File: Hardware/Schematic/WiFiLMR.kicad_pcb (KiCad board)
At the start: 2 copper layers, 26 parts, among them J1 Conn_01x12, J2 Conn_01x12, J3 JTAG, J4 Conn_02x04_Odd_Even, J5 Conn_02x02_Odd_Even, J6 Conn_01x12, J7 Conn_01x12, U1 TCA8418RTWR

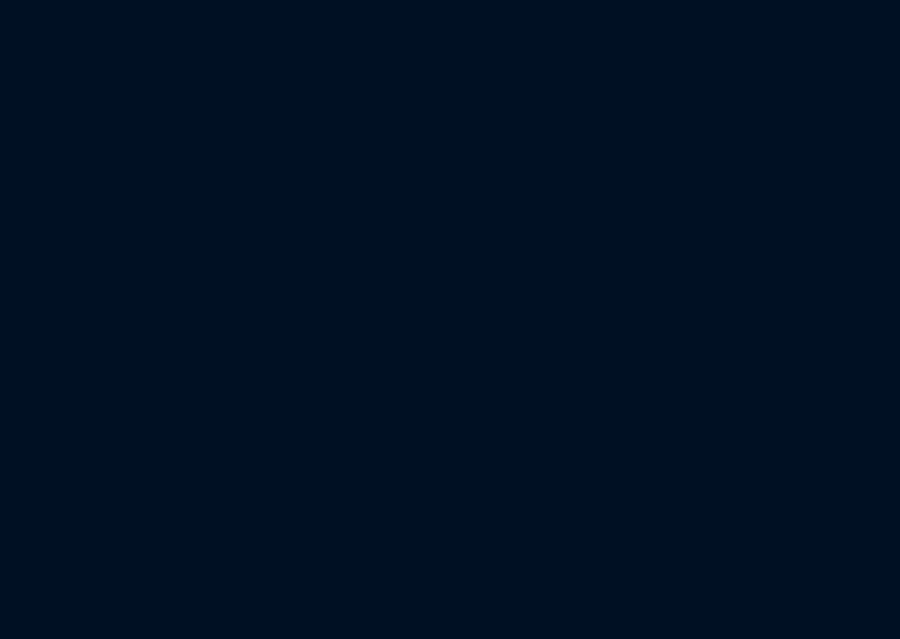
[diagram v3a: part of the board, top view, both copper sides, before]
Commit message: Added E-INK display connector and datasheet
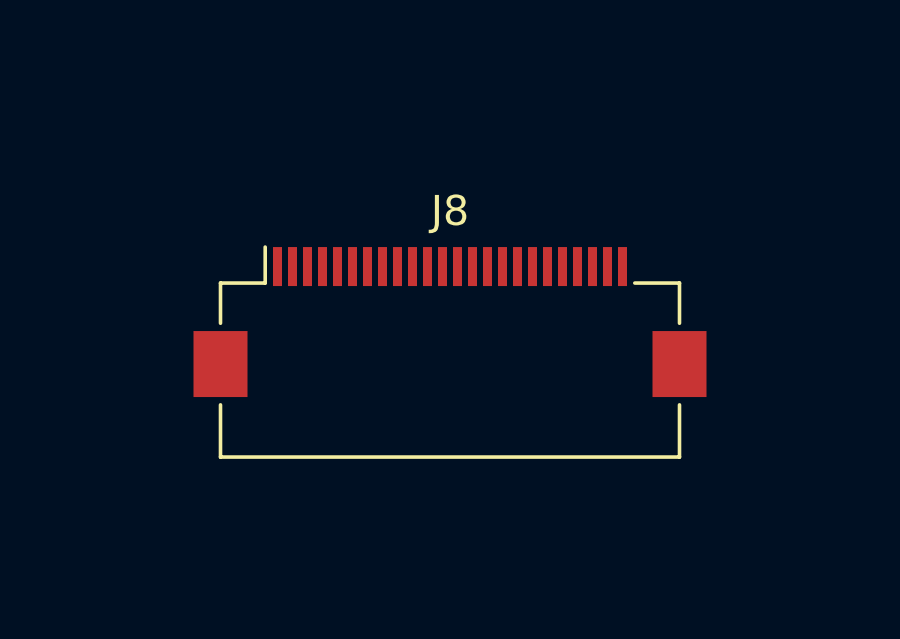
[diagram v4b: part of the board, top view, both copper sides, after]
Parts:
- added J8: Conn_01x24, Connector_FFC-FPC:Hirose_FH12-24S-0.5SH_1x24-1MP_P0.50mm_Horizontal, F.Cu at (74.9, 137.2)
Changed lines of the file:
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@@
     (tracks 0)
     (zones 0)
-    (modules 26)
-    (nets 103)
+    (modules 27)
+    (nets 127)
   )
   (page A4)
@@
   (net 101 /Keypad/COL9)
   (net 102 /Keypad/ROW7)
+  (net 103 "Net-(J8-Pad24)")
+  (net 104 "Net-(J8-Pad23)")
+  (net 105 "Net-(J8-Pad22)")
+  (net 106 "Net-(J8-Pad21)")
+  (net 107 "Net-(J8-Pad20)")
+  (net 108 "Net-(J8-Pad19)")
+  (net 109 "Net-(J8-Pad18)")
+  (net 110 "Net-(J8-Pad17)")
+  (net 111 "Net-(J8-Pad16)")
+  (net 112 "Net-(J8-Pad15)")
+  (net 113 "Net-(J8-Pad14)")
+  (net 114 "Net-(J8-Pad13)")
+  (net 115 "Net-(J8-Pad12)")
+  (net 116 "Net-(J8-Pad11)")
+  (net 117 "Net-(J8-Pad10)")
+  (net 118 "Net-(J8-Pad9)")
+  (net 119 "Net-(J8-Pad8)")
+  (net 120 "Net-(J8-Pad7)")
+  (net 121 "Net-(J8-Pad6)")
+  (net 122 "Net-(J8-Pad5)")
+  (net 123 "Net-(J8-Pad4)")
+  (net 124 "Net-(J8-Pad3)")
+  (net 125 "Net-(J8-Pad2)")
+  (net 126 "Net-(J8-Pad1)")
   (net_class Default "This is the default net class."
     (clearance 0.2)
@@
     (add_net "Net-(J7-Pad12)")
     (add_net "Net-(J7-Pad9)")
+    (add_net "Net-(J8-Pad1)")
+    (add_net "Net-(J8-Pad10)")
+    (add_net "Net-(J8-Pad11)")
+    (add_net "Net-(J8-Pad12)")
+    (add_net "Net-(J8-Pad13)")
+    (add_net "Net-(J8-Pad14)")
+    (add_net "Net-(J8-Pad15)")
+    (add_net "Net-(J8-Pad16)")
+    (add_net "Net-(J8-Pad17)")
+    (add_net "Net-(J8-Pad18)")
+    (add_net "Net-(J8-Pad19)")
+    (add_net "Net-(J8-Pad2)")
+    (add_net "Net-(J8-Pad20)")
+    (add_net "Net-(J8-Pad21)")
+    (add_net "Net-(J8-Pad22)")
+    (add_net "Net-(J8-Pad23)")
+    (add_net "Net-(J8-Pad24)")
+    (add_net "Net-(J8-Pad3)")
+    (add_net "Net-(J8-Pad4)")
+    (add_net "Net-(J8-Pad5)")
+    (add_net "Net-(J8-Pad6)")
+    (add_net "Net-(J8-Pad7)")
+    (add_net "Net-(J8-Pad8)")
+    (add_net "Net-(J8-Pad9)")
     (add_net "Net-(MODULE1-Pad1)")
     (add_net "Net-(MODULE1-Pad10)")
@@
     (add_net "Net-(U1-Pad5)")
   )
+  (module Connector_FFC-FPC:Hirose_FH12-24S-0.5SH_1x24-1MP_P0.50mm_Horizontal (layer F.Cu)
+    (at 74.93 137.16)
+    (descr "Molex FH12, FFC/FPC connector, FH12-24S-0.5SH, 24 Pins per row (https://www.hirose.com/product/en/products/FH12/FH12-24S-0.5SH(55)/), generated with kicad-footprint-generator")
+    (tags "connector Hirose  top entry")
+    (attr smd)
+    (fp_text reference J8 (at 0 -3.7) (layer F.SilkS)
+      (effects (font (size 1 1) (thickness 0.15)))
+    )
+    (fp_text value Conn_01x24 (at 0 5.6) (layer F.Fab)
+      (effects (font (size 1 1) (thickness 0.15)))
+    )
+    (fp_text user %R (at 0 3.7) (layer F.Fab)
+      (effects (font (size 1 1) (thickness 0.15)))
+    )
+    (fp_line (start 9.05 -3) (end -9.05 -3) (layer F.CrtYd) (width 0.05))
+    (fp_line (start 9.05 4.9) (end 9.05 -3) (layer F.CrtYd) (width 0.05))
+    (fp_line (start -9.05 4.9) (end 9.05 4.9) (layer F.CrtYd) (width 0.05))
+    (fp_line (start -9.05 -3) (end -9.05 4.9) (layer F.CrtYd) (width 0.05))
+    (fp_line (start -5.75 -0.492893) (end -5.25 -1.2) (layer F.Fab) (width 0.1))
+    (fp_line (start -6.25 -1.2) (end -5.75 -0.492893) (layer F.Fab) (width 0.1))
+    (fp_line (start -6.16 -1.3) (end -6.16 -2.5) (layer F.SilkS) (width 0.12))
+    (fp_line (start 7.65 4.5) (end 7.65 2.76) (layer F.SilkS) (width 0.12))
+    (fp_line (start -7.65 4.5) (end 7.65 4.5) (layer F.SilkS) (width 0.12))
+    (fp_line (start -7.65 2.76) (end -7.65 4.5) (layer F.SilkS) (width 0.12))
+    (fp_line (start 7.65 -1.3) (end 7.65 0.04) (layer F.SilkS) (width 0.12))
+    (fp_line (start 6.16 -1.3) (end 7.65 -1.3) (layer F.SilkS) (width 0.12))
+    (fp_line (start -7.65 -1.3) (end -7.65 0.04) (layer F.SilkS) (width 0.12))
+    (fp_line (start -6.16 -1.3) (end -7.65 -1.3) (layer F.SilkS) (width 0.12))
+    (fp_line (start 7.45 4.4) (end 0 4.4) (layer F.Fab) (width 0.1))
+    (fp_line (start 7.45 3.7) (end 7.45 4.4) (layer F.Fab) (width 0.1))
+    (fp_line (start 6.95 3.7) (end 7.45 3.7) (layer F.Fab) (width 0.1))
+    (fp_line (start 6.95 3.4) (end 6.95 3.7) (layer F.Fab) (width 0.1))
+    (fp_line (start 7.55 3.4) (end 6.95 3.4) (layer F.Fab) (width 0.1))
+    (fp_line (start 7.55 -1.2) (end 7.55 3.4) (layer F.Fab) (width 0.1))
+    (fp_line (start 0 -1.2) (end 7.55 -1.2) (layer F.Fab) (width 0.1))
+    (fp_line (start -7.45 4.4) (end 0 4.4) (layer F.Fab) (width 0.1))
+    (fp_line (start -7.45 3.7) (end -7.45 4.4) (layer F.Fab) (width 0.1))
+    (fp_line (start -6.95 3.7) (end -7.45 3.7) (layer F.Fab) (width 0.1))
+    (fp_line (start -6.95 3.4) (end -6.95 3.7) (layer F.Fab) (width 0.1))
+    (fp_line (start -7.55 3.4) (end -6.95 3.4) (layer F.Fab) (width 0.1))
+    (fp_line (start -7.55 -1.2) (end -7.55 3.4) (layer F.Fab) (width 0.1))
+    (fp_line (start 0 -1.2) (end -7.55 -1.2) (layer F.Fab) (width 0.1))
+    (pad 24 smd rect (at 5.75 -1.85) (size 0.3 1.3) (layers F.Cu F.Paste F.Mask)
+      (net 103 "Net-(J8-Pad24)"))
+    (pad 23 smd rect (at 5.25 -1.85) (size 0.3 1.3) (layers F.Cu F.Paste F.Mask)
+      (net 104 "Net-(J8-Pad23)"))
+    (pad 22 smd rect (at 4.75 -1.85) (size 0.3 1.3) (layers F.Cu F.Paste F.Mask)
+      (net 105 "Net-(J8-Pad22)"))
+    (pad 21 smd rect (at 4.25 -1.85) (size 0.3 1.3) (layers F.Cu F.Paste F.Mask)
+      (net 106 "Net-(J8-Pad21)"))
+    (pad 20 smd rect (at 3.75 -1.85) (size 0.3 1.3) (layers F.Cu F.Paste F.Mask)
+      (net 107 "Net-(J8-Pad20)"))
+    (pad 19 smd rect (at 3.25 -1.85) (size 0.3 1.3) (layers F.Cu F.Paste F.Mask)
+      (net 108 "Net-(J8-Pad19)"))
+    (pad 18 smd rect (at 2.75 -1.85) (size 0.3 1.3) (layers F.Cu F.Paste F.Mask)
+      (net 109 "Net-(J8-Pad18)"))
+    (pad 17 smd rect (at 2.25 -1.85) (size 0.3 1.3) (layers F.Cu F.Paste F.Mask)
+      (net 110 "Net-(J8-Pad17)"))
+    (pad 16 smd rect (at 1.75 -1.85) (size 0.3 1.3) (layers F.Cu F.Paste F.Mask)
+      (net 111 "Net-(J8-Pad16)"))
+    (pad 15 smd rect (at 1.25 -1.85) (size 0.3 1.3) (layers F.Cu F.Paste F.Mask)
+      (net 112 "Net-(J8-Pad15)"))
+    (pad 14 smd rect (at 0.75 -1.85) (size 0.3 1.3) (layers F.Cu F.Paste F.Mask)
+      (net 113 "Net-(J8-Pad14)"))
+    (pad 13 smd rect (at 0.25 -1.85) (size 0.3 1.3) (layers F.Cu F.Paste F.Mask)
+      (net 114 "Net-(J8-Pad13)"))
+    (pad 12 smd rect (at -0.25 -1.85) (size 0.3 1.3) (layers F.Cu F.Paste F.Mask)
+      (net 115 "Net-(J8-Pad12)"))
+    (pad 11 smd rect (at -0.75 -1.85) (size 0.3 1.3) (layers F.Cu F.Paste F.Mask)
+      (net 116 "Net-(J8-Pad11)"))
+    (pad 10 smd rect (at -1.25 -1.85) (size 0.3 1.3) (layers F.Cu F.Paste F.Mask)
+      (net 117 "Net-(J8-Pad10)"))
+    (pad 9 smd rect (at -1.75 -1.85) (size 0.3 1.3) (layers F.Cu F.Paste F.Mask)
+      (net 118 "Net-(J8-Pad9)"))
+    (pad 8 smd rect (at -2.25 -1.85) (size 0.3 1.3) (layers F.Cu F.Paste F.Mask)
+      (net 119 "Net-(J8-Pad8)"))
+    (pad 7 smd rect (at -2.75 -1.85) (size 0.3 1.3) (layers F.Cu F.Paste F.Mask)
+      (net 120 "Net-(J8-Pad7)"))
+    (pad 6 smd rect (at -3.25 -1.85) (size 0.3 1.3) (layers F.Cu F.Paste F.Mask)
+      (net 121 "Net-(J8-Pad6)"))
+    (pad 5 smd rect (at -3.75 -1.85) (size 0.3 1.3) (layers F.Cu F.Paste F.Mask)
+      (net 122 "Net-(J8-Pad5)"))
+    (pad 4 smd rect (at -4.25 -1.85) (size 0.3 1.3) (layers F.Cu F.Paste F.Mask)
+      (net 123 "Net-(J8-Pad4)"))
+    (pad 3 smd rect (at -4.75 -1.85) (size 0.3 1.3) (layers F.Cu F.Paste F.Mask)
+      (net 124 "Net-(J8-Pad3)"))
+    (pad 2 smd rect (at -5.25 -1.85) (size 0.3 1.3) (layers F.Cu F.Paste F.Mask)
+      (net 125 "Net-(J8-Pad2)"))
+    (pad 1 smd rect (at -5.75 -1.85) (size 0.3 1.3) (layers F.Cu F.Paste F.Mask)
+      (net 126 "Net-(J8-Pad1)"))
+    (pad MP smd rect (at -7.65 1.4) (size 1.8 2.2) (layers F.Cu F.Paste F.Mask))
+    (pad MP smd rect (at 7.65 1.4) (size 1.8 2.2) (layers F.Cu F.Paste F.Mask))
+    (model ${KISYS3DMOD}/Connector_FFC-FPC.3dshapes/Hirose_FH12-24S-0.5SH_1x24-1MP_P0.50mm_Horizontal.wrl
+      (at (xyz 0 0 0))
+      (scale (xyz 1 1 1))
+      (rotate (xyz 0 0 0))
+    )
+  )
   (module Button_Switch_SMD:SW_SPST_B3S-1000 (layer F.Cu)

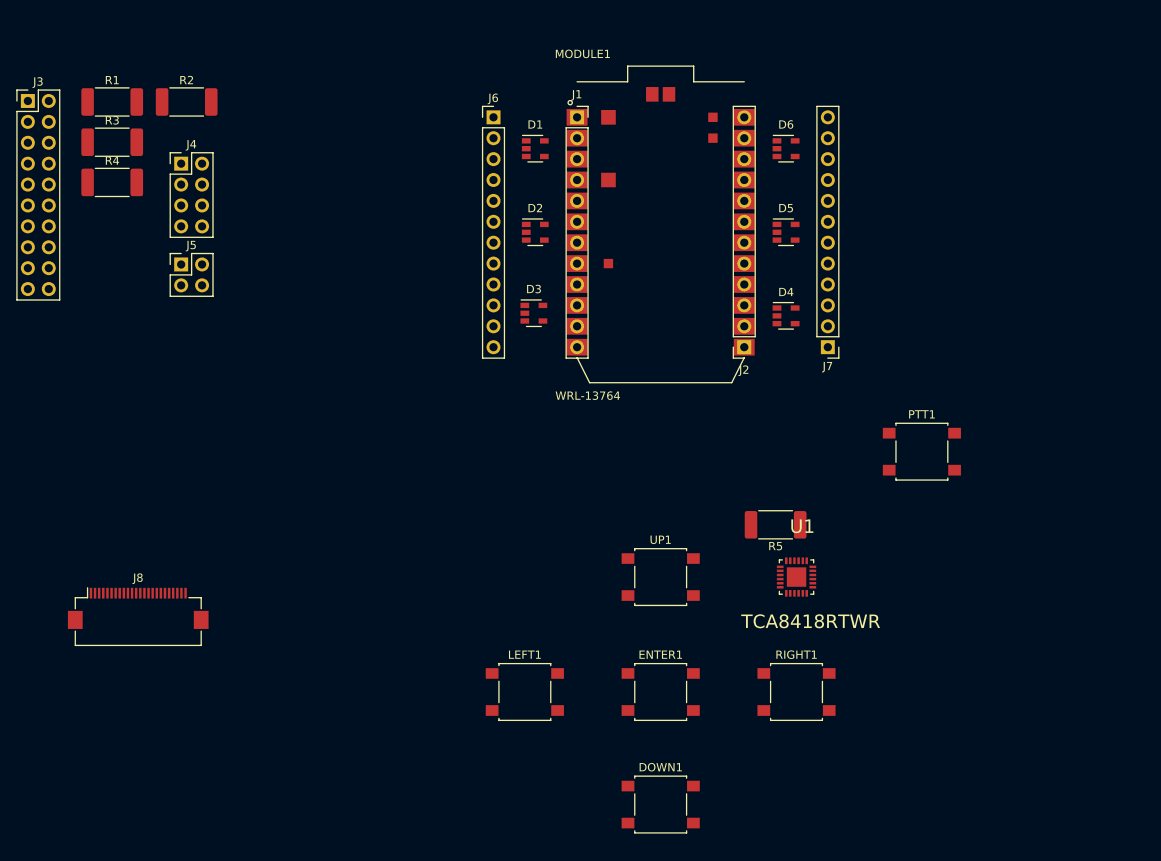
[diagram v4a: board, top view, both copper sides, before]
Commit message: Lots of schematic updates
Lots of stuff...

* Added a new 8-pin TVS diode array
* Finalized the display connector
* Corrected the net labels to global labels so they span across sheets
* Added a 5V linear voltage regulator and LEDs to debug power
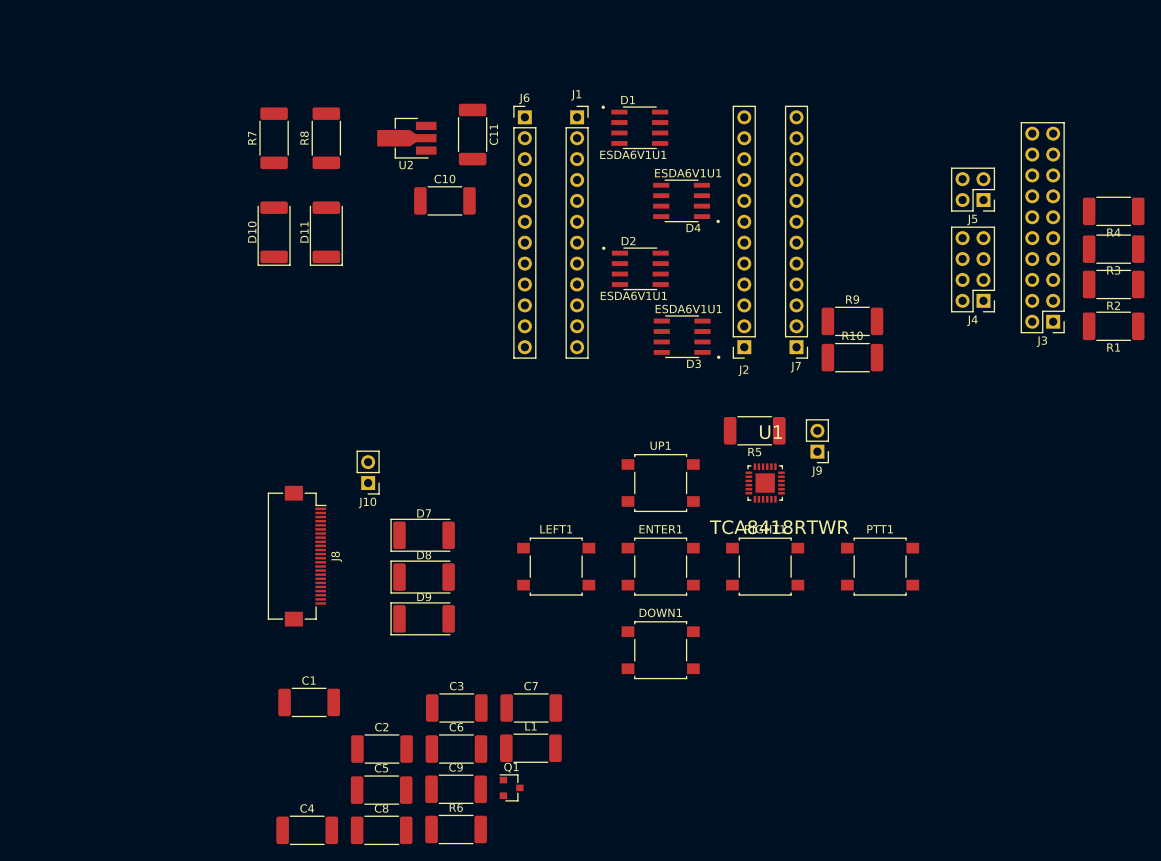
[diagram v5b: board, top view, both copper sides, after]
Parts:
- removed D5, D6: SP0504BAHT, Package_TO_SOT_SMD:SOT-23-5
- removed MODULE1: WRL-13764, WRL-13764:SPARKFUN_WRL-13764
- added C1: 0.1uF, Capacitor_SMD:C_2512_6332Metric_Pad1.52x3.35mm_HandSolder, F.Cu at (95.7, 148.6)
- added C10: 1uF, Capacitor_SMD:C_2512_6332Metric_Pad1.52x3.35mm_HandSolder, F.Cu at (112.2, 87.6)
- added C11: 1uF, Capacitor_SMD:C_2512_6332Metric_Pad1.52x3.35mm_HandSolder, F.Cu at (115.6, 79.6)
- added C2: 1uF, Capacitor_SMD:C_2512_6332Metric_Pad1.52x3.35mm_HandSolder, F.Cu at (104.6, 154.3)
- added C3: 4.7uF, Capacitor_SMD:C_2512_6332Metric_Pad1.52x3.35mm_HandSolder, F.Cu at (113.6, 149.3)
- added C4: 1uF, Capacitor_SMD:C_2512_6332Metric_Pad1.52x3.35mm_HandSolder, F.Cu at (95.5, 164.1)
- added C5: 1uF, Capacitor_SMD:C_2512_6332Metric_Pad1.52x3.35mm_HandSolder, F.Cu at (104.5, 159.2)
- added C6: 1uF, Capacitor_SMD:C_2512_6332Metric_Pad1.52x3.35mm_HandSolder, F.Cu at (113.6, 154.3)
- added C7: 1uF, Capacitor_SMD:C_2512_6332Metric_Pad1.52x3.35mm_HandSolder, F.Cu at (122.7, 149.3)
- added C8: 1uF, Capacitor_SMD:C_2512_6332Metric_Pad1.52x3.35mm_HandSolder, F.Cu at (104.5, 164.1)
- added C9: 1uF, Capacitor_SMD:C_2512_6332Metric_Pad1.52x3.35mm_HandSolder, F.Cu at (113.6, 159.1)
- added D10: LED, Diode_SMD:D_2512_6332Metric_Pad1.52x3.35mm_HandSolder, F.Cu at (91.4, 91.4)
- added D11: LED, Diode_SMD:D_2512_6332Metric_Pad1.52x3.35mm_HandSolder, F.Cu at (97.8, 91.4)
- added D7: D_Schottky, Diode_SMD:D_2512_6332Metric_Pad1.52x3.35mm_HandSolder, F.Cu at (109.7, 128.3)
- added D8: D_Schottky, Diode_SMD:D_2512_6332Metric_Pad1.52x3.35mm_HandSolder, F.Cu at (109.7, 133.3)
- added D9: D_Schottky, Diode_SMD:D_2512_6332Metric_Pad1.52x3.35mm_HandSolder, F.Cu at (109.7, 138.4)
- added J10: Conn_01x02, Connector_PinHeader_2.54mm:PinHeader_1x02_P2.54mm_Vertical, F.Cu at (102.9, 121.9)
- added J9: Conn_01x02, Connector_PinHeader_2.54mm:PinHeader_1x02_P2.54mm_Vertical, F.Cu at (157.5, 118.1)
- added L1: 10uH, Inductor_SMD:L_2512_6332Metric_Pad1.52x3.35mm_HandSolder, F.Cu at (122.7, 154.2)
- added Q1: Q_PJFET_GSD, Package_TO_SOT_SMD:SOT-23, F.Cu at (120.3, 159.0)
- added R10: R_Small_US, Resistor_SMD:R_2512_6332Metric_Pad1.52x3.35mm_HandSolder, F.Cu at (161.7, 106.7)
- added R6: 470mOhms, Resistor_SMD:R_2512_6332Metric_Pad1.52x3.35mm_HandSolder, F.Cu at (113.6, 164.0)
- added R7: R_Small_US, Resistor_SMD:R_2512_6332Metric_Pad1.52x3.35mm_HandSolder, F.Cu at (91.4, 80.0)
- added R8: R_Small_US, Resistor_SMD:R_2512_6332Metric_Pad1.52x3.35mm_HandSolder, F.Cu at (97.8, 80.0)
- added R9: R_Small_US, Resistor_SMD:R_2512_6332Metric_Pad1.52x3.35mm_HandSolder, F.Cu at (161.7, 102.3)
- added U2: L7805, Package_TO_SOT_SMD:SOT-89-3_Handsoldering, F.Cu at (108.0, 80.0)
- D1, D2, D3, D4: value SP0504BAHT -> ESDA6V1U1; footprint Package_TO_SOT_SMD:SOT-23-5 -> ESDA6V1U1:SOIC127P600X175-8N
- moved J3 127.5 mm to (186.1, 102.3), turned to 180 degrees
- moved R1 124.7 mm to (193.5, 102.9), turned to 180 degrees
- moved R3 122.4 mm to (193.5, 93.5), turned to 180 degrees
- moved R4 121.8 mm to (193.5, 88.9), turned to 180 degrees
- moved R2 114.8 mm to (193.5, 97.8), turned to 180 degrees
- moved J4 98.9 mm to (177.7, 99.8), turned to 180 degrees
- moved J5 97.8 mm to (177.7, 87.5), turned to 180 degrees
- moved J8 21.3 mm to (95.2, 130.8), turned to 270 degrees
- moved D4 18.9 mm to (141.0, 87.6), turned to 180 degrees
- moved DOWN1 18.8 mm to (138.4, 142.2)
- moved D3 18.2 mm to (141.0, 104.1), turned to 180 degrees
- moved LEFT1 15.7 mm to (125.7, 132.1)
- moved RIGHT1 15.7 mm to (151.1, 132.1)
- moved ENTER1 15.2 mm to (138.4, 132.1)
- moved PTT1 14.9 mm to (165.1, 132.1)
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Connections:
- net Net-(J8-Pad11) renamed /Display/DISP_DC
- net Net-(J8-Pad9) renamed /Display/DISP_BUSY
- D1 pad 1: Net-(D1-Pad1) -> +5V
- D1 pad 3: Net-(D1-Pad3) -> USART1_TX|TIM1_CH2
- D1 pad 4: /Particle_Connector/USART1_TX|TIM1_CH2 -> USART1_RX|TIM1_CH3
- D1 pad 5: /Particle_Connector/USART1_RX|TIM1_CH3 -> WKUP|ADC0|TIM5_CH1
- D2 pad 1: /Particle_Connector/WKUP|ADC0|TIM5_CH1 -> ADC7|SPI_MOSI|TIM3|CH2
- D2 pad 2: Earth -> ADC6|SPI_MISO|TIM3_CH1
- D2 pad 3: /Particle_Connector/ADC4|DAC1 -> ADC5|SPI_SCK|DAC2
- D2 pad 4: /Particle_Connector/ADC7|SPI_MOSI|TIM3_CH2 -> ADC12|SPI_SS
- D2 pad 5: /Particle_Connector/ADC6|SPI_MISO|TIM3_CH1 -> ADC13
- D3 pad 1: /Particle_Connector/ADC5|SPI_SCK|DAC2 -> SDA|TIM4_CH2
- D3 pad 2: Earth -> SCL|CAN2_TX|TIM4_CH1
- D3 pad 3: /Particle_Connector/ADC12|SPI_SS -> SPI1_MOSI|CAN2_RX|TIM3_CH2|I2S3_SD
- D3 pad 4: /Particle_Connector/ADC13 -> JTAG_TRST|SPI1_MISO|TIM3_CH1
- D3 pad 5: /Particle_Connector/ADC15 -> JTAG_TDO|SPI1_SCK|I2S3_SCK
- D4 pad 1: /Particle_Connector/SDA|TIM4_CH2 -> JTAG_TCK
- D4 pad 2: Earth -> JTAG_TMS
- D4 pad 3: /Particle_Connector/SCL|CAN2_TX|TIM4_CH1 -> Earth
- D4 pad 4: /Particle_Connector/SPI1_MOSI|CAN2_RX|TIM3_CH2|I2S3_SD -> +BATT
- D4 pad 5: /Particle_Connector/JTAG_TRST|SPI1_MISO|TIM3_CH1 -> RST
- J1 pad 1: Net-(J1-Pad1) -> +5V
- J1 pad 10: /Particle_Connector/ADC12|SPI_SS -> ADC12|SPI_SS
- J1 pad 11: /Particle_Connector/ADC13 -> ADC13
- J1 pad 12: /Particle_Connector/ADC15 -> ADC15
- J1 pad 3: /Particle_Connector/USART1_TX|TIM1_CH2 -> USART1_TX|TIM1_CH2
- J1 pad 4: /Particle_Connector/USART1_RX|TIM1_CH3 -> USART1_RX|TIM1_CH3
- J1 pad 5: /Particle_Connector/WKUP|ADC0|TIM5_CH1 -> WKUP|ADC0|TIM5_CH1
- J1 pad 6: /Particle_Connector/ADC4|DAC1 -> ADC4|DAC1
- J1 pad 7: /Particle_Connector/ADC7|SPI_MOSI|TIM3_CH2 -> ADC7|SPI_MOSI|TIM3|CH2
- J1 pad 8: /Particle_Connector/ADC6|SPI_MISO|TIM3_CH1 -> ADC6|SPI_MISO|TIM3_CH1
- J1 pad 9: /Particle_Connector/ADC5|SPI_SCK|DAC2 -> ADC5|SPI_SCK|DAC2
- J2 pad 1: /Particle_Connector/SDA|TIM4_CH2 -> SDA|TIM4_CH2
- J2 pad 11: /Particle_Connector/RST -> RST
- J2 pad 2: /Particle_Connector/SCL|CAN2_TX|TIM4_CH1 -> SCL|CAN2_TX|TIM4_CH1
- J2 pad 3: /Particle_Connector/SPI1_MOSI|CAN2_RX|TIM3_CH2|I2S3_SD -> SPI1_MOSI|CAN2_RX|TIM3_CH2|I2S3_SD
- J2 pad 4: /Particle_Connector/JTAG_TRST|SPI1_MISO|TIM3_CH1 -> JTAG_TRST|SPI1_MISO|TIM3_CH1
- J2 pad 5: /Particle_Connector/JTAG_TDO|SPI1_SCK|I2S3_SCK -> JTAG_TDO|SPI1_SCK|I2S3_SCK
- J2 pad 6: /Particle_Connector/JTAG_TDI|SPI1_SS|I2S3_WS -> JTAG_TDI|SPI1_SS|I2S3_WS
- J2 pad 7: /Particle_Connector/JTAG_TCK -> JTAG_TCK
- J2 pad 8: /Particle_Connector/JTAG_TMS -> JTAG_TMS
- J4 pad 1: /JTAG/JTAG_TRST|SPI1_MISO|TIM3_CH1 -> JTAG_TRST|SPI1_MISO|TIM3_CH1
- J4 pad 3: /JTAG/JTAG_TDI|SPI1_SS|I2S3_WS -> JTAG_TDI|SPI1_SS|I2S3_WS
- J4 pad 5: /JTAG/JTAG_TMS -> JTAG_TMS
- J4 pad 7: /JTAG/JTAG_TCK -> JTAG_TCK
- J5 pad 1: /JTAG/JTAG_TDO|SPI1_SCK|I2S3_SCK -> JTAG_TDO|SPI1_SCK|I2S3_SCK
- J5 pad 3: /JTAG/RST -> RST
- J6 pad 1: Net-(J6-Pad1) -> +5V
- J6 pad 10: /Particle_Connector/ADC12|SPI_SS -> ADC12|SPI_SS
- J6 pad 11: /Particle_Connector/ADC13 -> ADC13
- J6 pad 12: /Particle_Connector/ADC15 -> Net-(D2-Pad8)
- J6 pad 2: Net-(J6-Pad2) -> Earth
- J6 pad 3: /Particle_Connector/USART1_TX|TIM1_CH2 -> USART1_TX|TIM1_CH2
- J6 pad 4: /Particle_Connector/USART1_RX|TIM1_CH3 -> USART1_RX|TIM1_CH3
- J6 pad 5: /Particle_Connector/WKUP|ADC0|TIM5_CH1 -> WKUP|ADC0|TIM5_CH1
- J6 pad 6: /Particle_Connector/ADC4|DAC1 -> ADC4|DAC1
- J6 pad 7: /Particle_Connector/ADC7|SPI_MOSI|TIM3_CH2 -> ADC7|SPI_MOSI|TIM3|CH2
- J6 pad 8: /Particle_Connector/ADC6|SPI_MISO|TIM3_CH1 -> ADC6|SPI_MISO|TIM3_CH1
- J6 pad 9: /Particle_Connector/ADC5|SPI_SCK|DAC2 -> ADC5|SPI_SCK|DAC2
- J7 pad 1: /Particle_Connector/SDA|TIM4_CH2 -> SDA|TIM4_CH2
- J7 pad 10: Net-(J7-Pad10) -> +BATT
- J7 pad 11: /Particle_Connector/RST -> RST
- J7 pad 12: Net-(J7-Pad12) -> +3V3
- J7 pad 2: /Particle_Connector/SCL|CAN2_TX|TIM4_CH1 -> SCL|CAN2_TX|TIM4_CH1
- J7 pad 3: /Particle_Connector/SPI1_MOSI|CAN2_RX|TIM3_CH2|I2S3_SD -> SPI1_MOSI|CAN2_RX|TIM3_CH2|I2S3_SD
- J7 pad 4: /Particle_Connector/JTAG_TRST|SPI1_MISO|TIM3_CH1 -> JTAG_TRST|SPI1_MISO|TIM3_CH1
- J7 pad 5: /Particle_Connector/JTAG_TDO|SPI1_SCK|I2S3_SCK -> JTAG_TDO|SPI1_SCK|I2S3_SCK
- J7 pad 6: /Particle_Connector/JTAG_TDI|SPI1_SS|I2S3_WS -> JTAG_TDI|SPI1_SS|I2S3_WS
- J7 pad 7: /Particle_Connector/JTAG_TCK -> JTAG_TCK
- J7 pad 8: /Particle_Connector/JTAG_TMS -> JTAG_TMS
- J7 pad 9: Net-(J7-Pad9) -> Earth
- J8 pad 10: Net-(J8-Pad10) -> RST
- J8 pad 12: Net-(J8-Pad12) -> ADC12|SPI_SS
- J8 pad 13: Net-(J8-Pad13) -> ADC5|SPI_SCK|DAC2
- J8 pad 14: Net-(J8-Pad14) -> ADC7|SPI_MOSI|TIM3|CH2
- J8 pad 15: Net-(J8-Pad15) -> Net-(C1-Pad1)
- J8 pad 16: Net-(J8-Pad16) -> Net-(C1-Pad1)
- J8 pad 17: Net-(J8-Pad17) -> Earth
- J8 pad 8: Net-(J8-Pad8) -> Earth
- R5 pad 1: +3V3 -> Net-(J9-Pad2)
- U1 pad 20: /Keypad/RST -> RST
- U1 pad 21: +3V3 -> Net-(J9-Pad2)
- U1 pad 22: /Keypad/SDA|TIM4_CH2 -> SDA|TIM4_CH2
- U1 pad 23: /Keypad/SCL|CAN2_TX|TIM4_CH1 -> SCL|CAN2_TX|TIM4_CH1
